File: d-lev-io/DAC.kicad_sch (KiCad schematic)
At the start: 0 parts

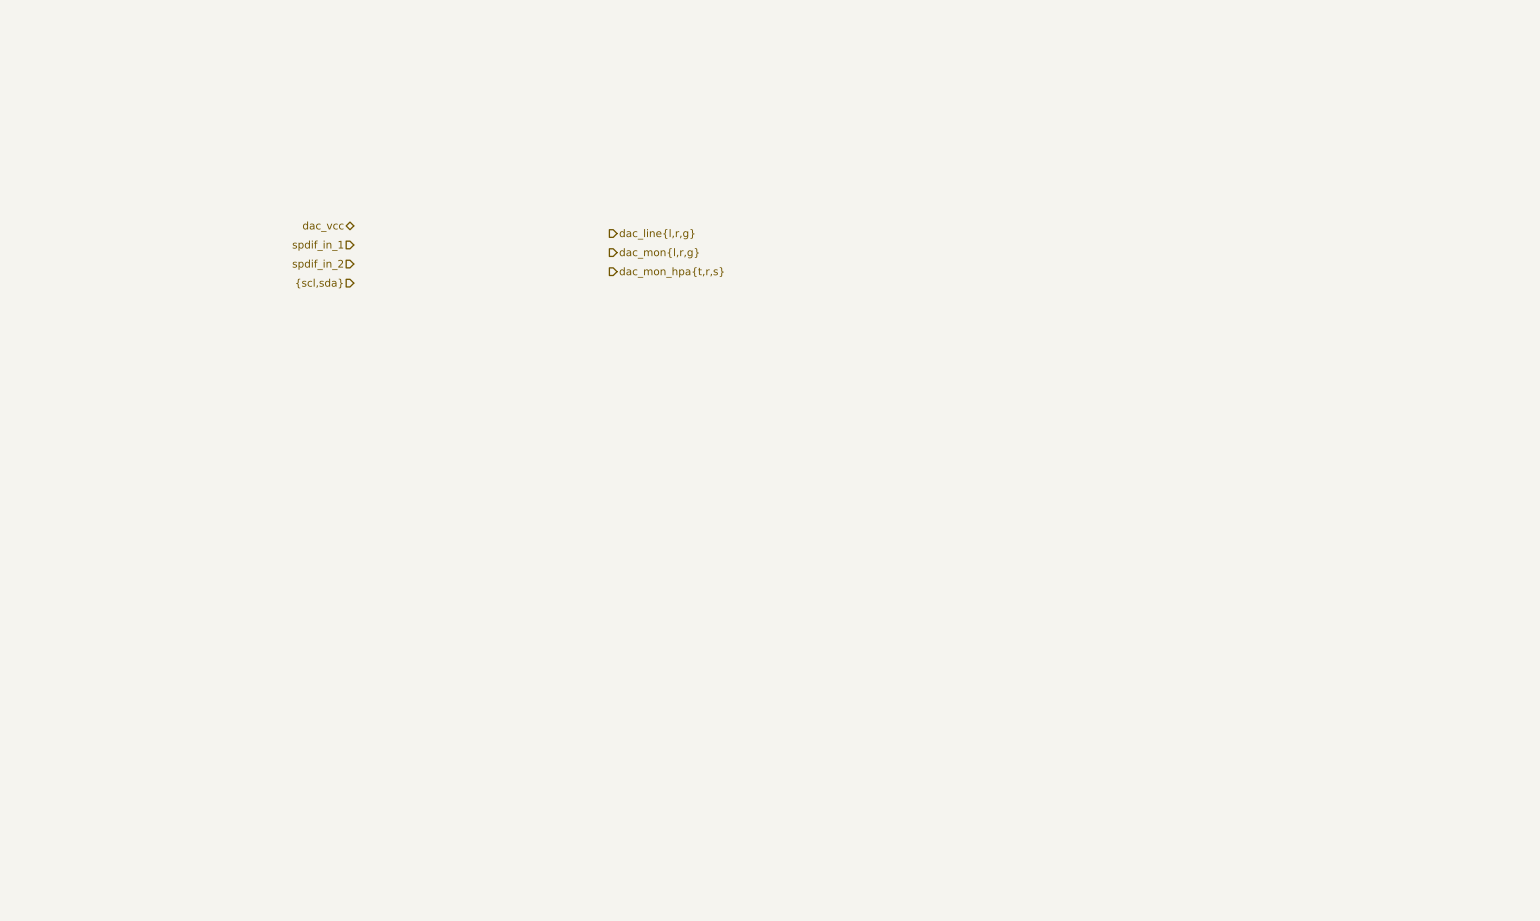
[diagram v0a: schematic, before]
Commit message: Added DAC schematic to I/O board
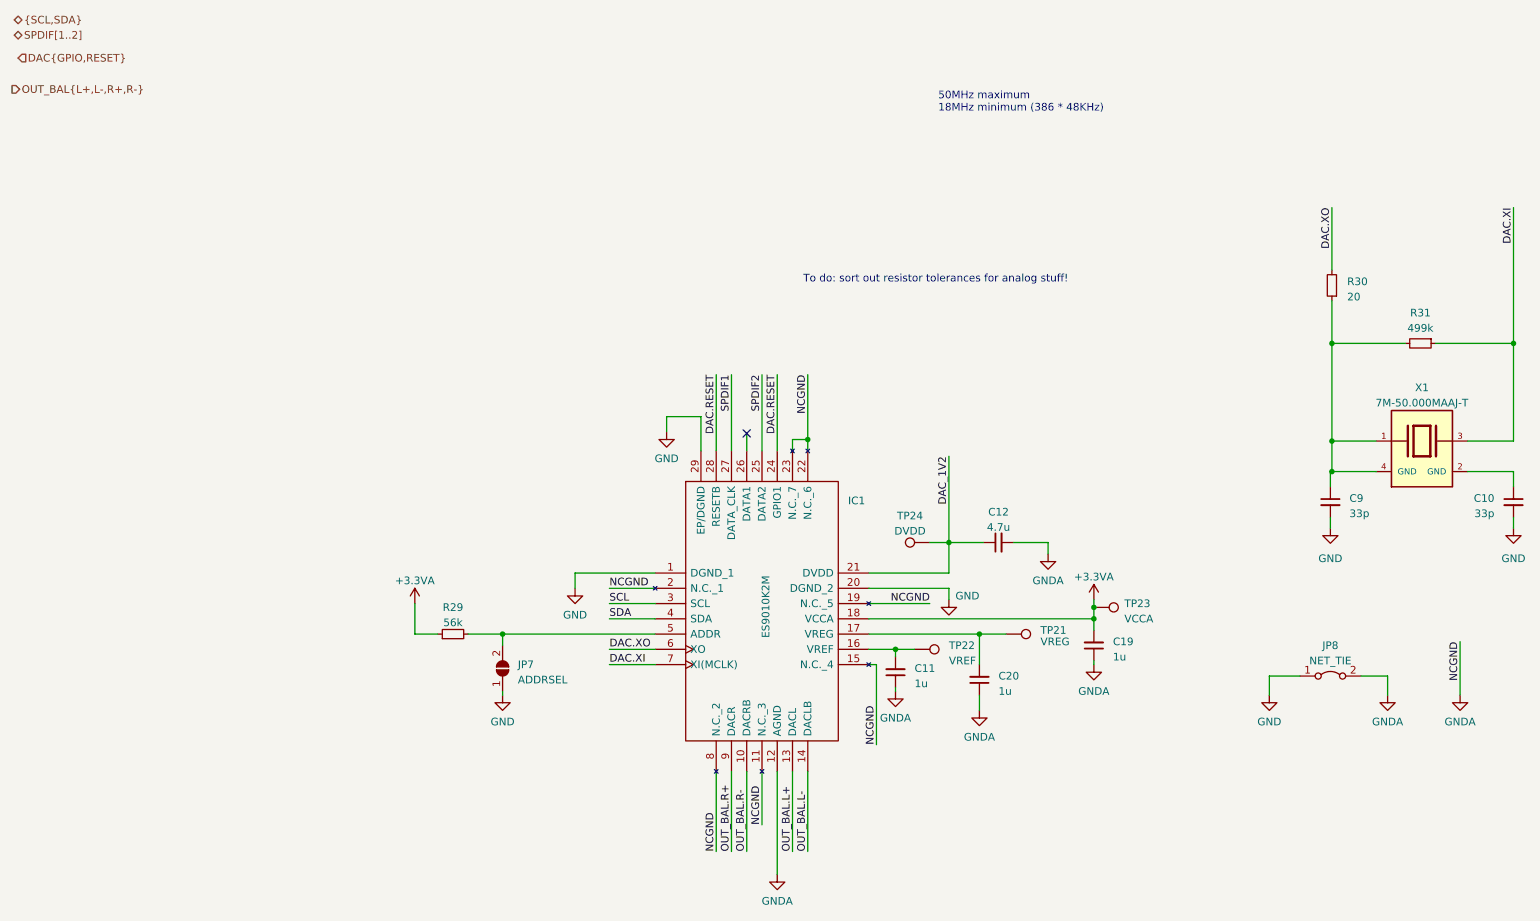
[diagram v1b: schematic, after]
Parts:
- added C10, C9: 33p, Capacitor_SMD:C_0603_1608Metric, symbol Device:C_Small
- added C11, C19, C20: 1u, Capacitor_SMD:C_0603_1608Metric, symbol Device:C_Small
- added C12: 4.7u, Capacitor_SMD:C_0603_1608Metric, symbol Device:C_Small
- added IC1: ES9010K2M, ess-dac:QFN50P500X500X90-29N-D, symbol ess_dac:ES9010K2M
- added JP7: ADDRSEL, Jumper:SolderJumper-2_P1.3mm_Bridged_RoundedPad1.0x1.5mm, symbol Jumper:SolderJumper_2_Open
- added JP8: NET_TIE, Jumper:SolderJumper-2_P1.3mm_Bridged_RoundedPad1.0x1.5mm, symbol Jumper:Jumper_2_Bridged
- added R29: 56k, Resistor_SMD:R_0603_1608Metric, symbol Device:R_Small
- added R30: 20, Resistor_SMD:R_0603_1608Metric, symbol Device:R_Small
- added R31: 499k, Resistor_SMD:R_0603_1608Metric, symbol Device:R_Small
- added TP21: VREG, TestPoint:TestPoint_Pad_D1.5mm, symbol Connector:TestPoint
- added TP22: VREF, TestPoint:TestPoint_Pad_D1.5mm, symbol Connector:TestPoint
- added TP23: VCCA, TestPoint:TestPoint_Pad_D1.5mm, symbol Connector:TestPoint
- added TP24: DVDD, TestPoint:TestPoint_Pad_D1.5mm, symbol Connector:TestPoint
- added X1: 7M-50.000MAAJ-T, ess-dac:XTAL_7M-50.000MAAJ-T, symbol ess_dac:7M-50.000MAAJ-T
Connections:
- new net: C11.2, IC1.16 (VREF), TP22.1
- new net: C20.2, IC1.17 (VREG), TP21.1
- new net: IC1.5 (ADDR), JP7.2 (B), R29.2
- new net: C10.1, X1.2 (GND)
- new net: C9.1, R30.1, R31.2, X1.1, X1.4 (GND)
- new net +3.3VA: C19.2, IC1.18 (VCCA), R29.1, TP23.1
- new net DAC.RESET: IC1.24 (GPIO1), IC1.28 (RESETB)
- new net DAC.XI: IC1.7 (XI(MCLK)), R31.1, X1.3
- new net DAC.XO: IC1.6 (XO), R30.2
- new net DAC_1V2: C12.1, IC1.21 (DVDD), TP24.1
- new net GND: C10.2, C9.2, IC1.1 (DGND_1), IC1.20 (DGND_2), IC1.29 (EP/DGND), JP7.1 (A), JP8.1 (A)
- new net GNDA: C11.1, C12.2, C19.1, C20.1, IC1.11 (N.C._3), IC1.12 (AGND), IC1.15 (N.C._4), IC1.19 (N.C._5), IC1.2 (N.C._1), IC1.22 (N.C._6), IC1.23 (N.C._7), IC1.8 (N.C._2), JP8.2 (B)
- new net OUT_BAL.L+: IC1.13 (DACL)
- new net OUT_BAL.L-: IC1.14 (DACLB)
- new net OUT_BAL.R+: IC1.9 (DACR)
- new net OUT_BAL.R-: IC1.10 (DACRB)
- new net SCL: IC1.3 (SCL)
- new net SDA: IC1.4 (SDA)
- new net SPDIF1: IC1.27 (DATA_CLK)
- new net SPDIF2: IC1.25 (DATA2)
- no-connect marks 0 -> 1
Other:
- note added: "50MHz maximum 18MHz minimum (386 * 48KHz)"
- note added: "To do: sort out resistor tolerances for analog stuff!"

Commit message: add headphone amp
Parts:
- removed JP8: NET_TIE, Jumper:SolderJumper-2_P1.3mm_Bridged_RoundedPad1.0x1.5mm, symbol Jumper:Jumper_2_Bridged
- added C28, C30, C33, C34: .47u, Capacitor_SMD:C_0603_1608Metric, symbol Device:C_Small
- added C31, C35, C36, C39: 1u, Capacitor_SMD:C_0603_1608Metric, symbol Device:C_Small
- added C38: 0.1u, Capacitor_SMD:C_0603_1608Metric, symbol Device:C_Small
- added IC3: MAX97220AETE+T, theremin:QFN50P300X300X80-17N, symbol assorted:MAX97220AETE+T
- added J6: MIDI_OUT_JACK, Connector_Audio:Jack_3.5mm_CUI_SJ-3523-SMT_Horizontal, symbol Connector:AudioJack3
- added NT1, NT2: NetTie_2, NetTie:NetTie-2_SMD_Pad0.5mm, symbol Device:NetTie_2
- added R19: 100k, Resistor_SMD:R_0603_1608Metric, symbol Device:R_Small
- added R42, R44: 0, Resistor_SMD:R_0603_1608Metric, symbol Device:R_Small
- added RIN1, RIN2, RIN3, RIN4: 10k, Resistor_SMD:R_0603_1608Metric, symbol Device:R_Small
- added RV2: 20K, symbol Device:R_Potentiometer_Dual
- C10, C9, R30, R31: Tolerance (none) -> 1%
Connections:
- net +3.3VA: now also R19.2
- net DAC.RESET: no longer IC1.24 (GPIO1)
- net GND: now also NT2.1
- net GNDA: now also C31.1, C36.2, C38.2, C39.2, IC3.3 (PGND), NT1.2, NT2.2, RV2.3, RV2.6
- net OUT_BAL.L+: now also C28.1
- net OUT_BAL.L-: now also C30.1
- net OUT_BAL.R+: now also C33.1
- net OUT_BAL.R-: now also C34.1
- new net: C33.2, RIN4.1
- new net: C28.2, RIN2.1
- new net: C30.2, RIN1.1
- new net: C34.2, RIN3.1
- new net: J6.R, R42.1
- new net: C38.1, IC3.11 (BIAS)
- new net: C35.1, IC3.2 (C1P)
- new net: C35.2, IC3.4 (C1N)
- new net: C31.2, IC3.5 (PVSS)
- new net: J6.T, R44.1
- new net AMP_PVDD: C36.1, C39.1, IC3.1 (PVDD), IC3.13 (SVDD), IC3.9 (SVDD2)
- new net AMP_SGND: IC3.6 (SGND), J6.S, NT1.1
- new net DAC.GPIO: IC1.24 (GPIO1)
- new net HPA_SHDN: IC3.16 (~{SHDN}), R19.1
- new net IN_BAL.L+: IC3.15 (INL+), RIN2.2
- new net IN_BAL.L-: IC3.14 (INL-), RIN1.2, RV2.2
- new net IN_BAL.R+: IC3.7 (INR+), RIN4.2
- new net IN_BAL.R-: IC3.8 (INR-), RIN3.2, RV2.5
- new net OUT_SE.L: IC3.12 (OUTL), R44.2, RV2.1
- new net OUT_SE.R: IC3.10 (OUTR), R42.2, RV2.4
- no-connect marks 1 -> 2
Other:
- note added: "[ ] Connect PGND and SGND together at a single point on the PCB. [ ] Connect all components associated with the charge pump (C31 and C35) to the PGND plane. [ ] Connect PVDD and SVDD together at the device. [ ] Place capacitors C31 and C35 as close as possible to the device. [ ] Ensure the PCB layout is partisioned so that the large switching currents in the ground plane do not return through SGN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"
- moved on the sheet: C10, C11, C12, C19, C20, C9, IC1, JP7, R29, R30, R31, TP21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

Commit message: io board more analog schematic capture
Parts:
- removed C33, C34: .47u, Capacitor_SMD:C_0603_1608Metric, symbol Device:C_Small
- removed J6: MIDI_OUT_JACK, Connector_Audio:Jack_3.5mm_CUI_SJ-3523-SMT_Horizontal, symbol Connector:AudioJack3
- removed R42, R44: 0, Resistor_SMD:R_0603_1608Metric, symbol Device:R_Small
- removed RIN1, RIN2, RIN3, RIN4: 10k, Resistor_SMD:R_0603_1608Metric, symbol Device:R_Small
- removed RV2: 20K, symbol Device:R_Potentiometer_Dual
- added C29, C32: .47u, Capacitor_SMD:C_0603_1608Metric, symbol Device:C_Small
- IC3: value MAX97220AETE+T -> MAX97220C/MAX97220D
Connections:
- net +3.3VA: no longer R19.2
- net AMP_PVDD: now also R19.2
- net IN_BAL.L+: now also C28.2
- net IN_BAL.L-: now also C30.2
- net IN_BAL.R+: now also C29.2
- net IN_BAL.R-: now also C32.2
- net OUT_BAL.R+: now also C29.1
- net OUT_BAL.R-: now also C32.1
- net DAC.GPIO renamed DAC_GPIO
- net DAC.RESET renamed DAC_RESET
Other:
- note added: "In to amp"
- note added: "Out from DAC"
- note added: "Todo: sort out resistor tolerances for DAC"
- note removed: "To do: sort out resistor tolerances for analog stuff!"
- moved on the sheet: C28, C30, C36, C38, NT1

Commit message: many board updates
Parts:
- removed JP7: ADDRSEL, Jumper:SolderJumper-2_P1.3mm_Bridged_RoundedPad1.0x1.5mm, symbol Jumper:SolderJumper_2_Open
- added C43: 1u, Capacitor_SMD:C_0603_1608Metric, symbol Device:C_Small
- added R43: 0, Resistor_SMD:R_0603_1608Metric, symbol Device:R_Small
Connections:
- net AMP_PVDD is gone; now on net +3.3VA: C36.1, C39.1, IC3.1 (PVDD), IC3.13 (SVDD), IC3.9 (SVDD2), R19.2
- net DAC.XI: now also C10.1
- net DAC.XO: now also R31.2
- net DAC_RESET: now also C43.2
- net GND: now also X1.2 (GND), X1.4 (GND), C43.1, R43.1
- net at IC1.5 (ADDR), R29.2: now also R43.2
- net at C9.1, R30.1, X1.1: no longer R31.2, X1.4 (GND)
- net AMP_SGND renamed OUT_SE_G
- net OUT_SE.L renamed OUT_SE_L
- net OUT_SE.R renamed OUT_SE_R
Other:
- moved on the sheet: C10, C9, R30, X1

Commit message: more routing
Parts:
- removed NT1: NetTie_2, NetTie:NetTie-2_SMD_Pad0.5mm, symbol Device:NetTie_2
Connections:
- net OUT_SE_G is gone; now on net GNDA: IC3.6 (SGND)
- net SPDIF1: now also IC1.25 (DATA2); no longer IC1.27 (DATA_CLK)
- net SPDIF2: now also IC1.27 (DATA_CLK); no longer IC1.25 (DATA2)
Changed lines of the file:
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@@
     (stroke (width 0) (type default))
   )
-  (wire (pts (xy 242.57 136.525) (xy 255.27 136.525))
+  (wire (pts (xy 242.57 136.525) (xy 265.43 136.525))
     (stroke (width 0) (type default))
   )
@@
   )
   (wire (pts (xy 125.73 48.895) (xy 120.015 48.895))
-    (stroke (width 0) (type default))
-  )
-  (wire (pts (xy 260.35 136.525) (xy 265.43 136.525))
     (stroke (width 0) (type default))
   )
@@
     (effects (font (size 1.27 1.27)) (justify right bottom))
   )
-  (label "SPDIF2" (at 88.9 20.32 270) (fields_autoplaced)
+  (label "SPDIF2" (at 83.82 20.32 270) (fields_autoplaced)
     (effects (font (size 1.27 1.27)) (justify right bottom))
   )
@@
     (effects (font (size 1.27 1.27)) (justify left bottom))
   )
-  (label "SPDIF1" (at 83.82 20.32 270) (fields_autoplaced)
+  (label "SPDIF1" (at 88.9 20.32 270) (fields_autoplaced)
     (effects (font (size 1.27 1.27)) (justify right bottom))
   )
@@
         )
       )
-    )
-  )
-  (symbol (lib_id "Device:NetTie_2") (at 257.81 136.525 0) (unit 1)
-    (in_bom no) (on_board yes) (dnp no)
-    (property "Reference" "NT1" (at 257.81 133.096 0)
-      (effects (font (size 1.27 1.27)))
-    )
-    (property "Value" "NetTie_2" (at 257.81 135.636 0)
-      (effects (font (size 1.27 1.27)))
-    )
-    (property "Footprint" "NetTie:NetTie-2_SMD_Pad0.5mm" (at 257.81 136.525 0)
-      (effects (font (size 1.27 1.27)) hide)
-    )
-    (property "Datasheet" "~" (at 257.81 136.525 0)
-      (effects (font (size 1.27 1.27)) hide)
-    )
-    (pin "1")
-    (pin "2")
-    (instances
-      (project "d-lev-io"
-        (path "/9261a07b-ae4a-4d72-8042-ea097cd0e5ed/a27f70fd-d508-47b8-a0c3-100551b81610"
-          (reference "NT1") (unit 1)
-        )
-      )

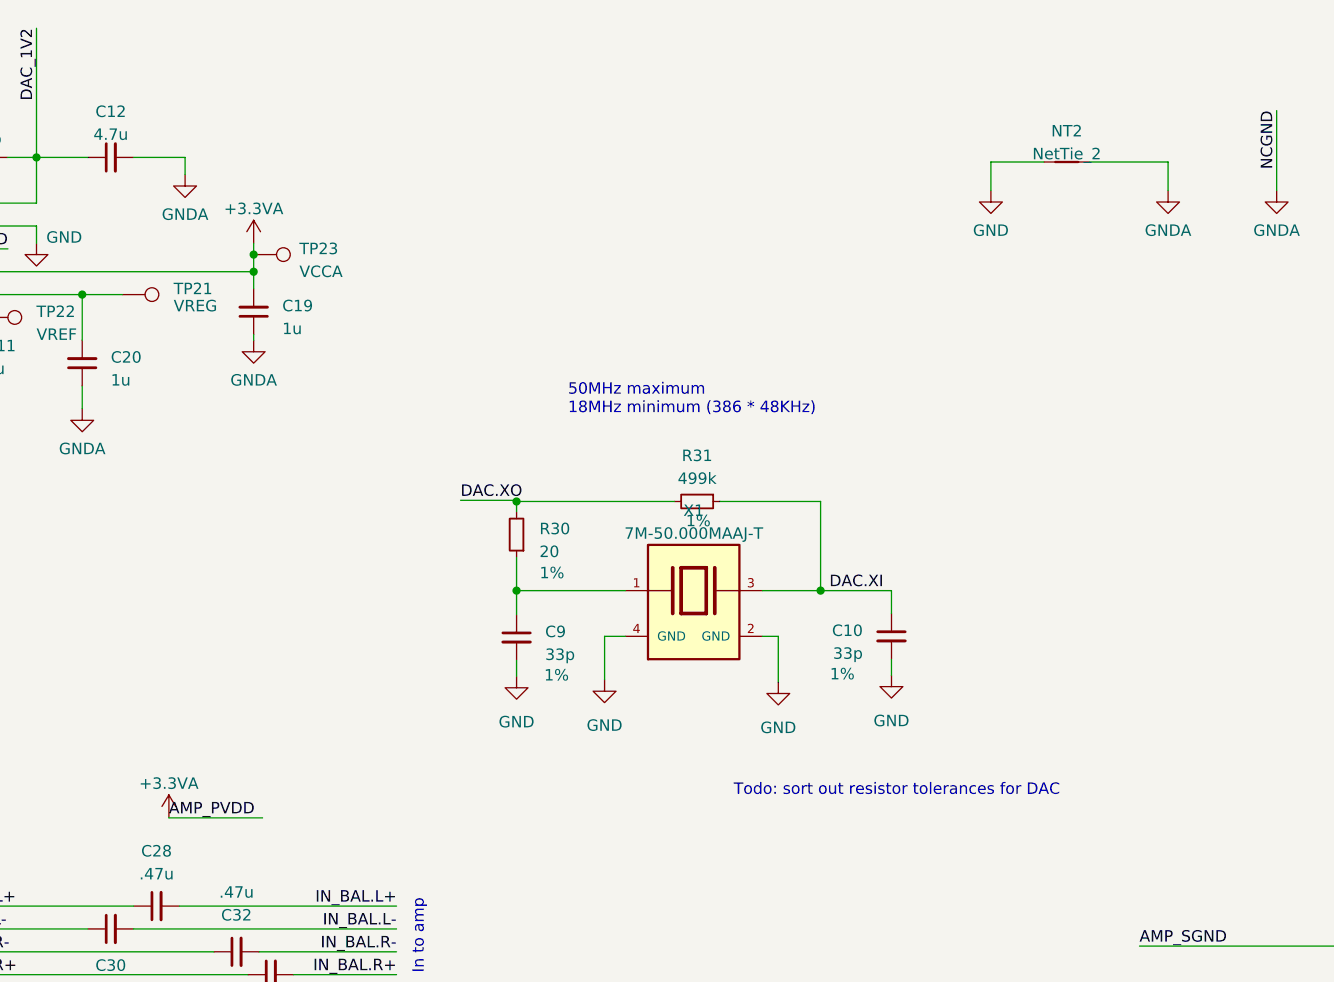
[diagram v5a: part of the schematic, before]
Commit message: Routed IO board
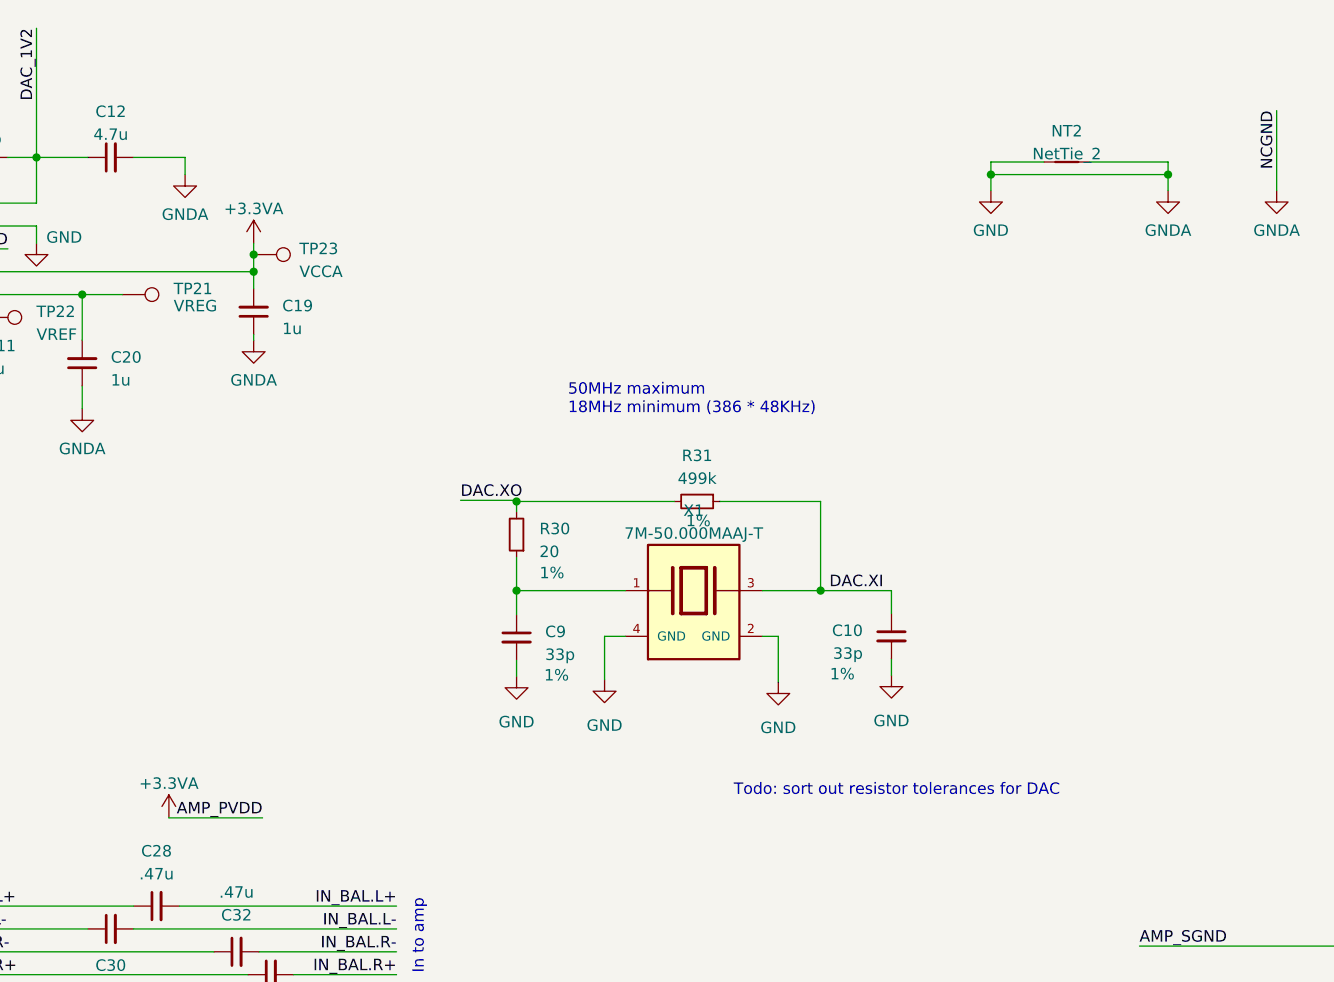
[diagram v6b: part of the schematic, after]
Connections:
- net GNDA is gone; now on net GND: C11.1, C12.2, C19.1, C20.1, C31.1, C36.2, C38.2, C39.2, IC1.11 (N.C._3), IC1.12 (AGND), IC1.15 (N.C._4), IC1.19 (N.C._5), IC1.2 (N.C._1), IC1.22 (N.C._6), IC1.23 (N.C._7), IC1.8 (N.C._2), IC3.3 (PGND), IC3.6 (SGND), NT2.2
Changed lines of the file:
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@@
   (junction (at 120.015 48.895) (diameter 0) (color 0 0 0 0)
   )
+  (junction (at 226.06 50.8) (diameter 0) (color 0 0 0 0)
+  )
   (junction (at 125.095 64.135) (diameter 0) (color 0 0 0 0)
   )
   (junction (at 144.145 61.595) (diameter 0) (color 0 0 0 0)
+  )
+  (junction (at 245.745 50.8) (diameter 0) (color 0 0 0 0)
   )
   (junction (at 96.52 31.75) (diameter 0) (color 0 0 0 0)
@@
     (stroke (width 0) (type default))
   )
+  (wire (pts (xy 245.745 50.8) (xy 245.745 49.403))
+    (stroke (width 0) (type default))
+  )
   (wire (pts (xy 22.5666 131.064) (xy 35.052 131.064))
     (stroke (width 0) (type default))
@@
     (stroke (width 0) (type default))
   )
-  (wire (pts (xy 226.06 52.578) (xy 226.06 49.403))
+  (wire (pts (xy 226.06 49.403) (xy 226.06 50.8))
     (stroke (width 0) (type default))
   )
@@
     (stroke (width 0) (type default))
   )
+  (wire (pts (xy 226.06 50.8) (xy 226.06 52.578))
+    (stroke (width 0) (type default))
+  )
   (wire (pts (xy 93.98 100.33) (xy 93.98 86.995))
     (stroke (width 0) (type default))
@@
     (stroke (width 0) (type default))
   )
+  (wire (pts (xy 245.745 50.8) (xy 226.06 50.8))
+    (stroke (width 0) (type default))
+  )
   (wire (pts (xy 31.115 64.135) (xy 34.925 64.135))
     (stroke (width 0) (type default))
@@
     (stroke (width 0) (type default))
   )
-  (wire (pts (xy 245.745 52.578) (xy 245.745 49.403))
+  (wire (pts (xy 245.745 52.578) (xy 245.745 50.8))
     (stroke (width 0) (type default))
   )
@@
     (effects (font (size 1.27 1.27)) (justify left bottom))
   )
-  (label "AMP_PVDD" (at 134.7216 122.2756 0) (fields_autoplaced)
-    (effects (font (size 1.27 1.27)) (justify left bottom))
+  (label "AMP_PVDD" (at 145.1356 122.2756 180) (fields_autoplaced)
+    (effects (font (size 1.27 1.27)) (justify right bottom))
   )
   (label "AMP_PGND" (at 89.789 136.144 180) (fields_autoplaced)
